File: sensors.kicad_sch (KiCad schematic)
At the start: 44 parts, among them J401 ACC_INT1, J402 BME_SPI, J403 LUX_INT, U202 NUCLEO64-H503RB, U401 LSM6DS3, U402 BME280, U403 OPT4001, U404 INA2180A2, U406 YK16S-L7.2-B10Ka(32-8)-G-A29

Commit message: Finished the sourcing of the components
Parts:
- JP402: now left out of the parts list
- R403, R406: LCSC (none) -> C2090841
- R404, R407: LCSC (none) -> C3013349
- R405: LCSC (none) -> C3013345
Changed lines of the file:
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@@
 				)
 			)
-			(project ""
+			(project "Educational-Board_MainBoard"
 				(path "/835b4df9-7d62-45f4-81d2-5a64fbc86f3c/fff2b078-1c83-42d8-b24c-4d93ca90abbb"
 					(reference "U403")
@@
 				)
 			)
-			(project ""
+			(project "Educational-Board_MainBoard"
 				(path "/835b4df9-7d62-45f4-81d2-5a64fbc86f3c/fff2b078-1c83-42d8-b24c-4d93ca90abbb"
 					(reference "#PWR0425")
@@
 				)
 			)
-			(project ""
+			(project "Educational-Board_MainBoard"
 				(path "/835b4df9-7d62-45f4-81d2-5a64fbc86f3c/fff2b078-1c83-42d8-b24c-4d93ca90abbb"
 					(reference "J401")
@@
 			)
 		)
-		(property "LCSC" ""
+		(property "LCSC" "C3013349"
 			(at 72.39 161.29 90)
 			(effects
@@
 		)
 		(instances
-			(project ""
+			(project "Educational-Board_MainBoard"
 				(path "/835b4df9-7d62-45f4-81d2-5a64fbc86f3c/fff2b078-1c83-42d8-b24c-4d93ca90abbb"
 					(reference "U404")
@@
 				)
 			)
-			(project ""
+			(project "Educational-Board_MainBoard"
 				(path "/835b4df9-7d62-45f4-81d2-5a64fbc86f3c/fff2b078-1c83-42d8-b24c-4d93ca90abbb"
 					(reference "R401")
@@
 				)
 			)
-			(project ""
+			(project "Educational-Board_MainBoard"
 				(path "/835b4df9-7d62-45f4-81d2-5a64fbc86f3c/fff2b078-1c83-42d8-b24c-4d93ca90abbb"
 					(reference "U402")
@@
 				)
 			)
-			(project ""
+			(project "Educational-Board_MainBoard"
 				(path "/835b4df9-7d62-45f4-81d2-5a64fbc86f3c/fff2b078-1c83-42d8-b24c-4d93ca90abbb"
 					(reference "#PWR0432")
@@
 			)
 		)
+		(property "LCSC" "C2090841"
+			(at 66.04 161.29 90)
+			(effects
+				(font
+					(size 1.27 1.27)
+				)
+				(hide yes)
+			)
+		)
 		(pin "2"
 		)
@@
 				)
 			)
-			(project ""
+			(project "Educational-Board_MainBoard"
 				(path "/835b4df9-7d62-45f4-81d2-5a64fbc86f3c/fff2b078-1c83-42d8-b24c-4d93ca90abbb"
 					(reference "U406")
@@
 			)
 		)
-		(property "LCSC" ""
+		(property "LCSC" "C3013345"
 			(at 78.74 120.65 90)
 			(effects
@@
 		)
 		(instances
-			(project ""
+			(project "Educational-Board_MainBoard"
 				(path "/835b4df9-7d62-45f4-81d2-5a64fbc86f3c/fff2b078-1c83-42d8-b24c-4d93ca90abbb"
 					(reference "U404")
@@
 		(unit 1)
 		(exclude_from_sim no)
-		(in_bom yes)
+		(in_bom no)
 		(on_board yes)
 		(dnp yes)
@@
 			)
 		)
+		(property "LCSC" "C2090841"
+			(at 66.04 120.65 90)
+			(effects
+				(font
+					(size 1.27 1.27)
+				)
+				(hide yes)
+			)
+		)
 		(pin "2"
 		)
@@
 		)
 		(instances
-			(project ""
+			(project "Educational-Board_MainBoard"
 				(path "/835b4df9-7d62-45f4-81d2-5a64fbc86f3c/fff2b078-1c83-42d8-b24c-4d93ca90abbb"
 					(reference "JP410")
@@
 				)
 			)
-			(project ""
+			(project "Educational-Board_MainBoard"
 				(path "/835b4df9-7d62-45f4-81d2-5a64fbc86f3c/fff2b078-1c83-42d8-b24c-4d93ca90abbb"
 					(reference "J402")
@@
 		)
 		(instances
-			(project ""
+			(project "Educational-Board_MainBoard"
 				(path "/835b4df9-7d62-45f4-81d2-5a64fbc86f3c/fff2b078-1c83-42d8-b24c-4d93ca90abbb"
 					(reference "U404")
@@
 			)
 		)
-		(property "LCSC" ""
+		(property "LCSC" "C3013349"
 			(at 72.39 120.65 90)
 			(effects

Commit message: Started the checking of the components
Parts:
- C401, C402, C403, C404, C405, C406, C407, C408, C409, C410, C411, D401, D402, J401, J402, J403, JP401, JP402, JP403, JP404, JP405, JP406, JP407, JP408, JP409, JP410, JP411, JP412, JP413, JP414, JP415, R401, R402, R403, R406, U402, U404: Checked (none) -> OK
- U401: Checked (none) -> Maybe more power?

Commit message: Continued to check components footprints
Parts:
- R404, R405, R407, U403, U406: Checked (none) -> OK
- U401: Checked Maybe more power? -> E- Maybe more power?
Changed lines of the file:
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@@
 			)
 		)
-		(property "Checked" ""
+		(property "Checked" "OK"
 			(at 214.63 59.69 0)
 			(effects
@@
 			)
 		)
-		(property "Checked" "Maybe more power?"
+		(property "Checked" "E- Maybe more power?"
 			(at 64.77 59.69 0)
 			(effects
@@
 			)
 		)
-		(property "Checked" ""
+		(property "Checked" "OK"
 			(at 72.39 161.29 90)
 			(effects
@@
 			)
 		)
-		(property "Checked" ""
+		(property "Checked" "OK"
 			(at 227.33 124.46 0)
 			(effects
@@
 			)
 		)
-		(property "Checked" ""
+		(property "Checked" "OK"
 			(at 78.74 120.65 90)
 			(effects
@@
 			)
 		)
-		(property "Checked" ""
+		(property "Checked" "OK"
 			(at 72.39 120.65 90)
 			(effects

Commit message: Changed two connectors
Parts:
- U202: footprint ProjectConnectors:Nucleo64 -> ProjectConnectors:Nucleo64_ST-Morpho
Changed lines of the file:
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@@
 			)
 		)
-		(property "Footprint" "ProjectConnectors:Nucleo64"
+		(property "Footprint" "ProjectConnectors:Nucleo64_ST-Morpho"
 			(at 75.438 149.098 0)
 			(effects
@@
 			)
 		)
-		(property "Footprint" "ProjectConnectors:Nucleo64"
+		(property "Footprint" "ProjectConnectors:Nucleo64_ST-Morpho"
 			(at 75.438 189.738 0)
 			(effects

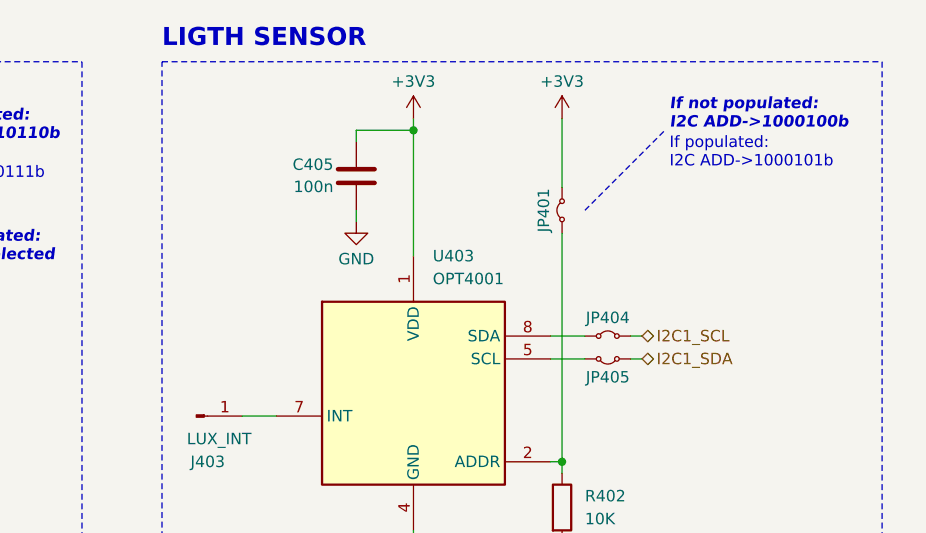
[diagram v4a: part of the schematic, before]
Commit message: Started the floorplan + added the Power LED
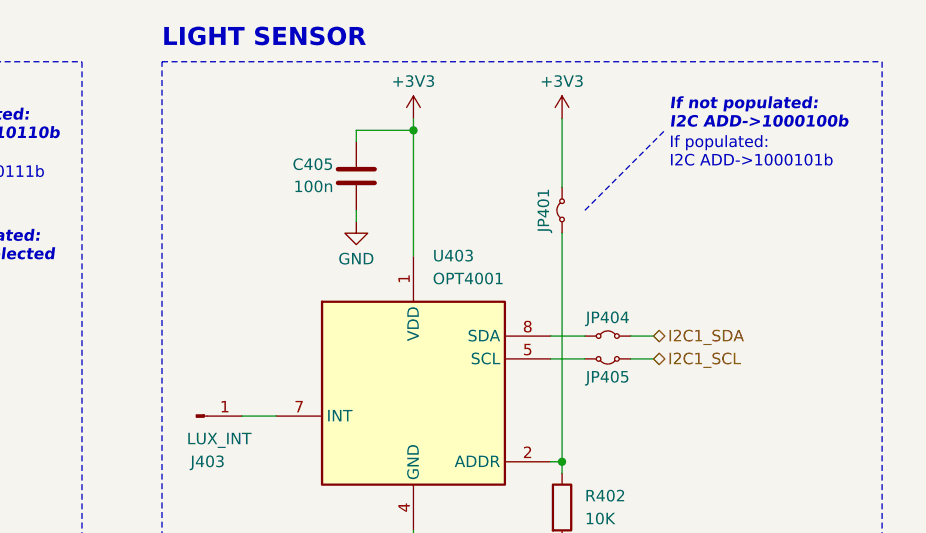
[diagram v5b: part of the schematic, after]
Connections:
- net I2C1_SCL: now also JP405.2 (B); no longer JP404.2 (B)
- net I2C1_SDA: now also JP404.2 (B); no longer JP405.2 (B)
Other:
- note added: "LIGHT SENSOR"
- note removed: "LIGTH SENSOR"
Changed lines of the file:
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@@
 		)
 	)
-	(text "LIGTH SENSOR"
+	(text "LIGHT SENSOR"
 		(exclude_from_sim no)
 		(at 186.69 20.32 0)
@@
 	(wire
 		(pts
-			(xy 238.76 53.34) (xy 240.03 53.34)
-		)
-		(stroke
-			(width 0)
-			(type default)
-		)
-	)
-	(wire
-		(pts
 			(xy 144.78 29.21) (xy 144.78 38.1)
 		)
@@
 	(wire
 		(pts
+			(xy 238.76 55.88) (xy 241.3 55.88)
+		)
+		(stroke
+			(width 0)
+			(type default)
+		)
+	)
+	(wire
+		(pts
 			(xy 210.82 124.46) (xy 213.36 124.46)
 		)
@@
 	(wire
 		(pts
-			(xy 238.76 55.88) (xy 240.03 55.88)
-		)
-		(stroke
-			(width 0)
-			(type default)
-		)
-	)
-	(wire
-		(pts
 			(xy 210.82 124.46) (xy 210.82 125.73)
 		)
@@
 		(pts
 			(xy 134.62 39.37) (xy 134.62 40.64)
+		)
+		(stroke
+			(width 0)
+			(type default)
+		)
+	)
+	(wire
+		(pts
+			(xy 238.76 53.34) (xy 241.3 53.34)
 		)
 		(stroke
@@
 	(hierarchical_label "I2C1_SCL"
 		(shape bidirectional)
-		(at 240.03 53.34 0)
+		(at 241.3 55.88 0)
 		(effects
 			(font
@@
 	(hierarchical_label "I2C1_SDA"
 		(shape bidirectional)
-		(at 240.03 55.88 0)
+		(at 241.3 53.34 0)
 		(effects
 			(font

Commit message: Continued the floor plan
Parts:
- U401: Checked E- Maybe more power? -> E- Maybe more power?, Footprint to add silkscreen axes
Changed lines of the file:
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@@
 			)
 		)
-		(property "Checked" "E- Maybe more power?"
+		(property "Checked" "E- Maybe more power?, Footprint to add silkscreen axes"
 			(at 64.77 59.69 0)
 			(effects

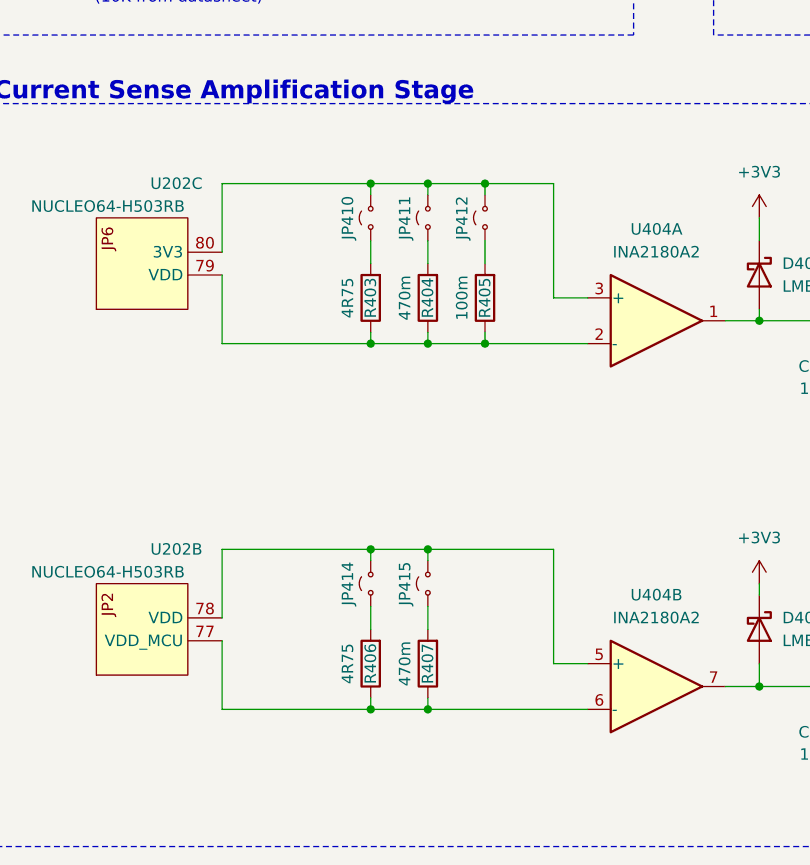
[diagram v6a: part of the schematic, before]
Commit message: Roued the majority of the nets of the POWER IO
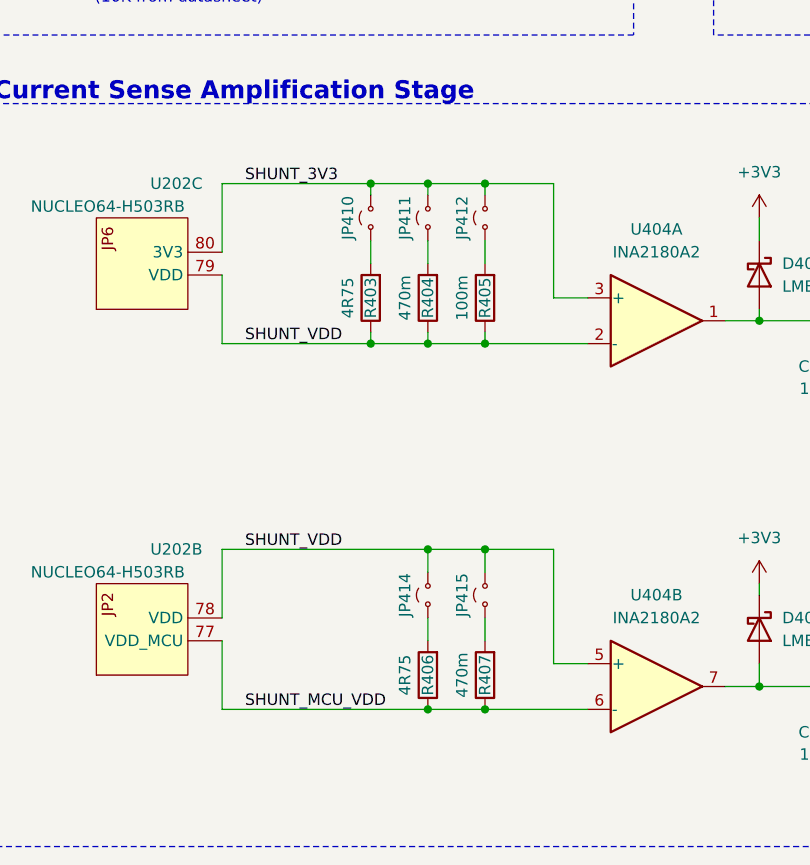
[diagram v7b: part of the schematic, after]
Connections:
- net SHUNT_MCU_VDD: now reaches R406.1, R407.1, U202.77 (VDD_MCU), U404.6 (-)
- net SHUNT_VDD: now reaches R403.1, R404.1, R405.1, U202.79 (VDD), U404.2 (-)
- net SHUNT_VDD: now also JP414.2 (B), JP415.2 (B), U202.78 (VDD), U404.5 (+)
- net SHUNT_3V3: now reaches JP410.2 (B), JP411.2 (B), JP412.2 (B), U202.80 (3V3), U404.3 (+)
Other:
- moved on the sheet: JP414, JP415, R406, R407
